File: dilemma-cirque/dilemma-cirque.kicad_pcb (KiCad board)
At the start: 2 copper layers, 37 x 45.1 mm, 9 parts, among them J1 CirqueDB

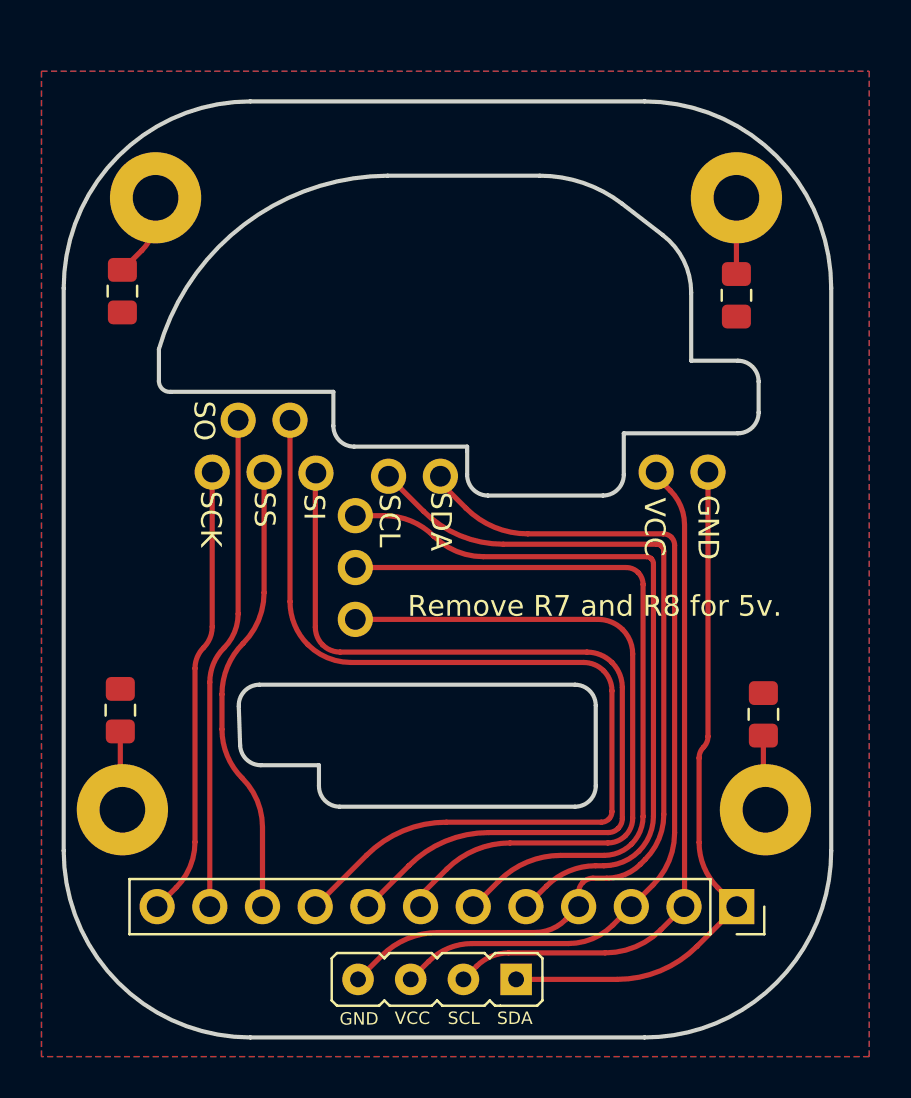
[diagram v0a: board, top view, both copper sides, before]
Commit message: Footprint library created, CirqueDB more compact
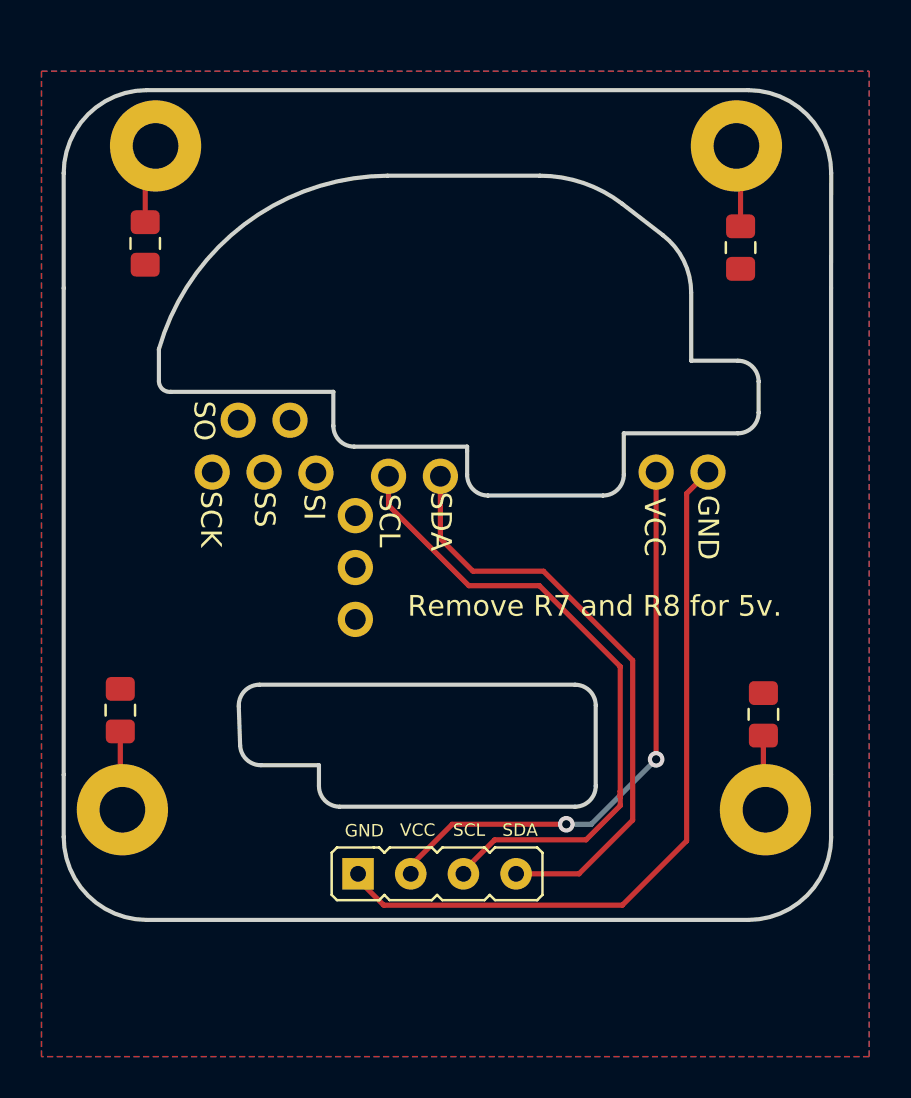
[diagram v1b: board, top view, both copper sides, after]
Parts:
- J1: footprint BK-CirqueDB:CirqueDB-BK -> BK-CirqueDB:CirqueDB_compact-BK
- moved FB2 2.55 mm to (131.5, 75.8)
- moved H1 2.50 mm to (160.0, 71.1)
- moved H2 2.50 mm to (132.0, 71.1)
- moved FB1 2.31 mm to (160.2, 76.0)
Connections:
- FB1 pad 1: (no net) -> Net-(FB1-Pad1)
- FB2 pad 1: (no net) -> Net-(FB2-Pad1)
- FB3 pad 1: (no net) -> Net-(FB3-Pad1)
- FB4 pad 1: (no net) -> Net-(FB4-Pad1)
- J1 pad 1: SDA -> GND
- J1 pad 2: SCL -> VCC
- J1 pad 3: VCC -> SDA
- J1 pad 4: GND -> SCL
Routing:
- net DR: track 48.5 -> 0.00 mm
- net MOSI: track 44.0 -> 0.00 mm
- net B2: track 35.6 -> 0.00 mm
- net B1: track 35.4 -> 0.00 mm
- net B3: track 34.5 -> 0.00 mm
- net MISO: track 23.8 -> 0.00 mm
- net SS: track 21.9 -> 0.00 mm
- net SCK: track 21.8 -> 0.00 mm
- net VCC: track 42.6 -> 28.2 mm, vias 0 -> 2
- net GND: track 45.9 -> 36.1 mm
- net SDA: track 33.6 -> 29.1 mm
- net SCL: track 33.6 -> 31.8 mm
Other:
- board size 37 x 45.1 mm -> 37 x 40 mm

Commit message: silkscreen
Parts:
- added G***: LOGO, local-libraries:LOGO, B.Cu at (134.5, 92.7)
- added kibuzzard-61F01A92: G***, local-libraries:kibuzzard-61F01A92, F.Cu at (145.3, 70.0)
- added kibuzzard-61F01A92: G***, local-libraries:kibuzzard-61F01A92, B.Cu at (155.2, 90.5)
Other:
- board text added: "0.1a"
- board text added: "BastardKB x Freznel"

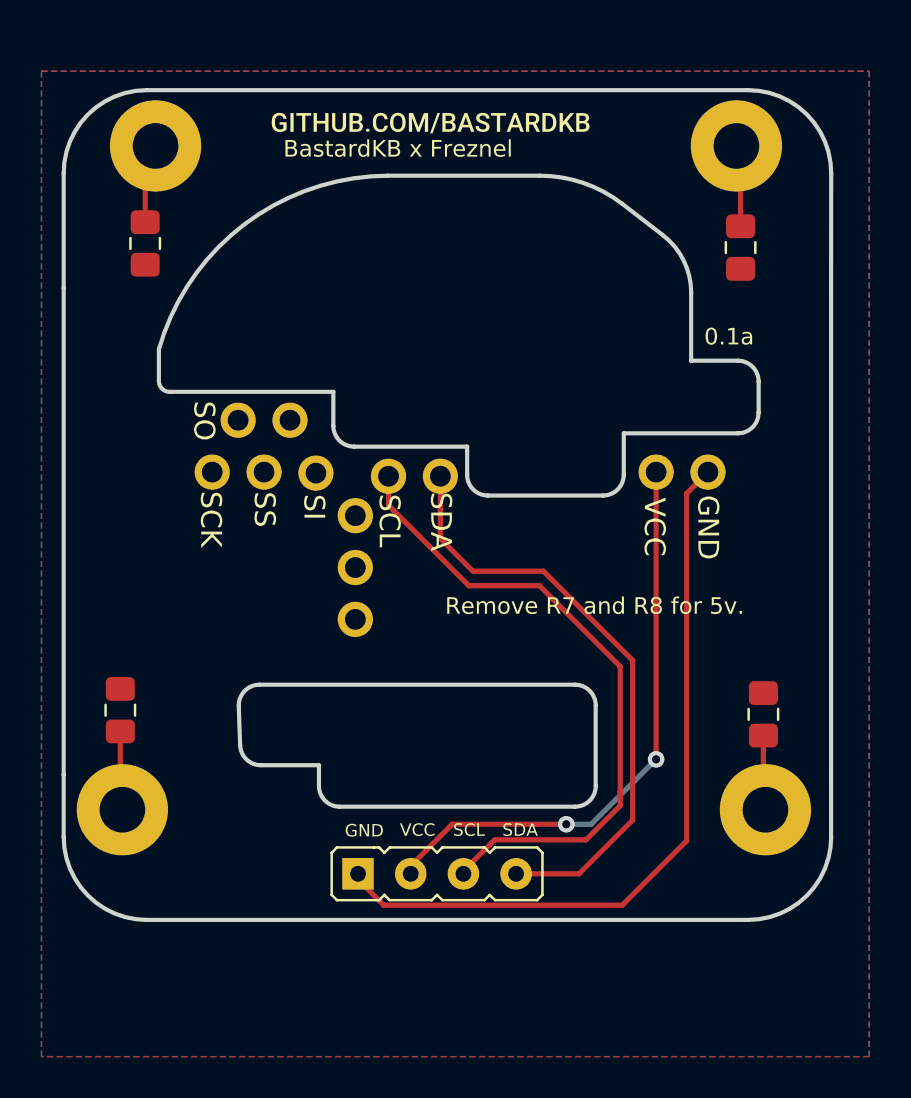
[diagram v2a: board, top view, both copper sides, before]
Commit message: M2 to M3
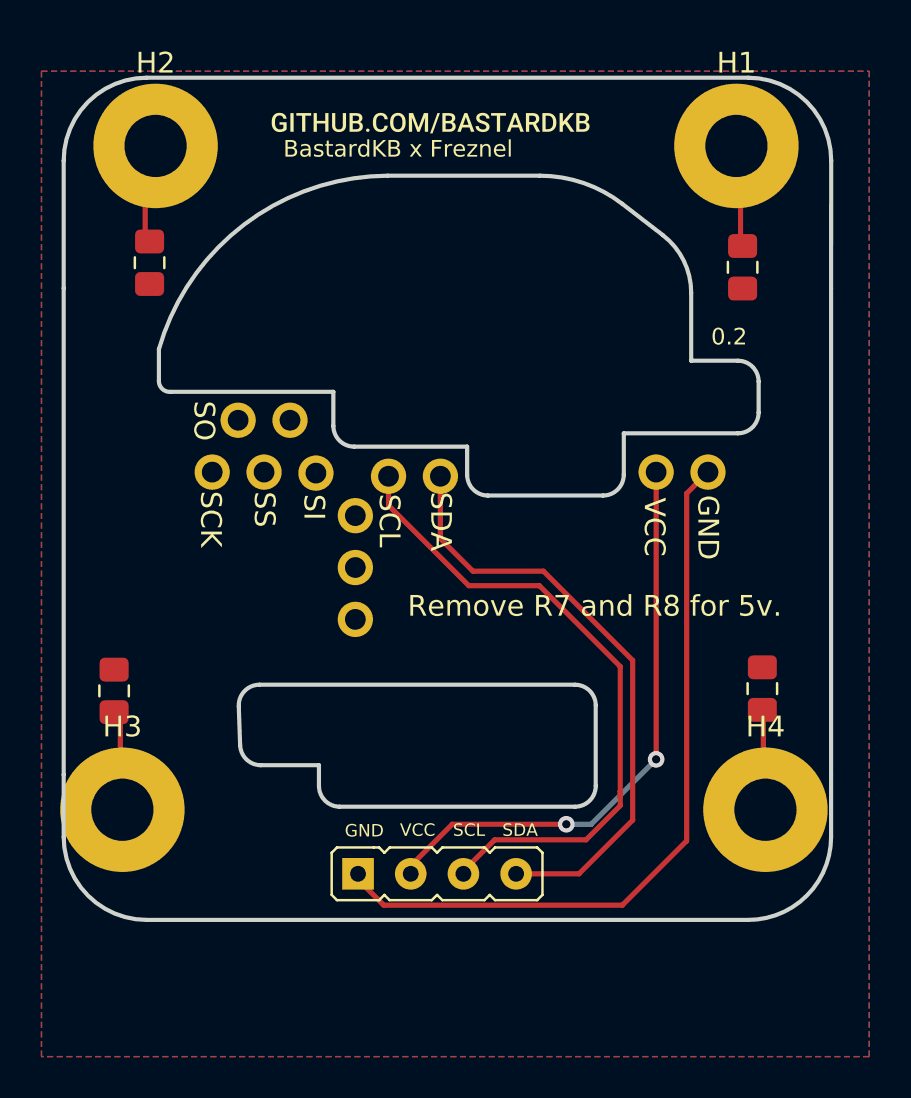
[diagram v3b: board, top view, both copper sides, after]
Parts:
- FB1, FB2, FB3, FB4: footprint BK-CirqueDB:L_0805_2012Metric_Pad1.15x1.40mm_HandSolder -> BKCirqueDB:L_0805_2012Metric_Pad1.15x1.40mm_HandSolder
- H1, H2, H3, H4: footprint BK-CirqueDB:MountingHole_2.2mm_M2_Pad -> MountingHole:MountingHole_3mm_Pad
- J1: footprint BK-CirqueDB:CirqueDB_compact-BK -> BKCirqueDB:CirqueDB_compact-BK
- moved FB4 1.24 mm to (161.2, 97.3)
- moved FB3 0.98 mm to (130.0, 97.4)
- moved FB1 0.96 mm to (160.3, 77.0)
- moved FB2 0.95 mm to (131.7, 76.7)
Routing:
- net Net-(FB4-Pad1): track 3.62 -> 4.88 mm
- net Net-(FB3-Pad1): track 3.82 -> 4.87 mm
- net Net-(FB2-Pad1): track 3.88 -> 4.90 mm
- net Net-(FB1-Pad1): track 3.96 -> 4.95 mm
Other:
- board size 37 x 40 mm -> 37 x 40.6 mm
- board text added: "0.2"
- board text removed: "0.1a"
